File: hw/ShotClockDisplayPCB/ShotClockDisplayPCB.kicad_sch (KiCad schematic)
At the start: 0 parts

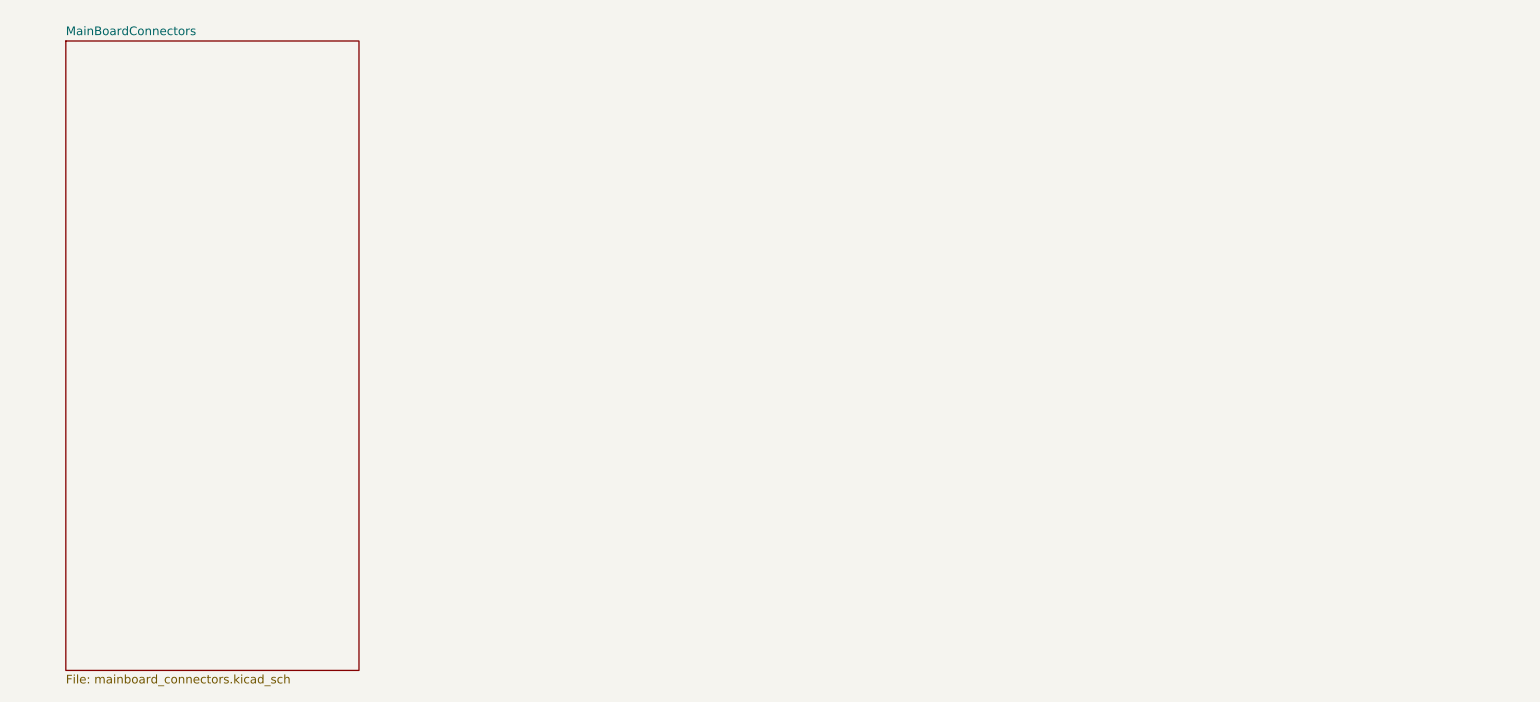
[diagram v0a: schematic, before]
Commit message: Started on second PCB, and added 5V regulator
5V regulator added to main pcb for the segment displays, using same TPS63000 chip, but with a different selector resistor to choose for 5V

Added second project to contain the display PCBA design.

Calculated the current usage of the displays with different current limiting resistors on the LEDs.

Calculated the  current limit resistors for transistors behind LEDs
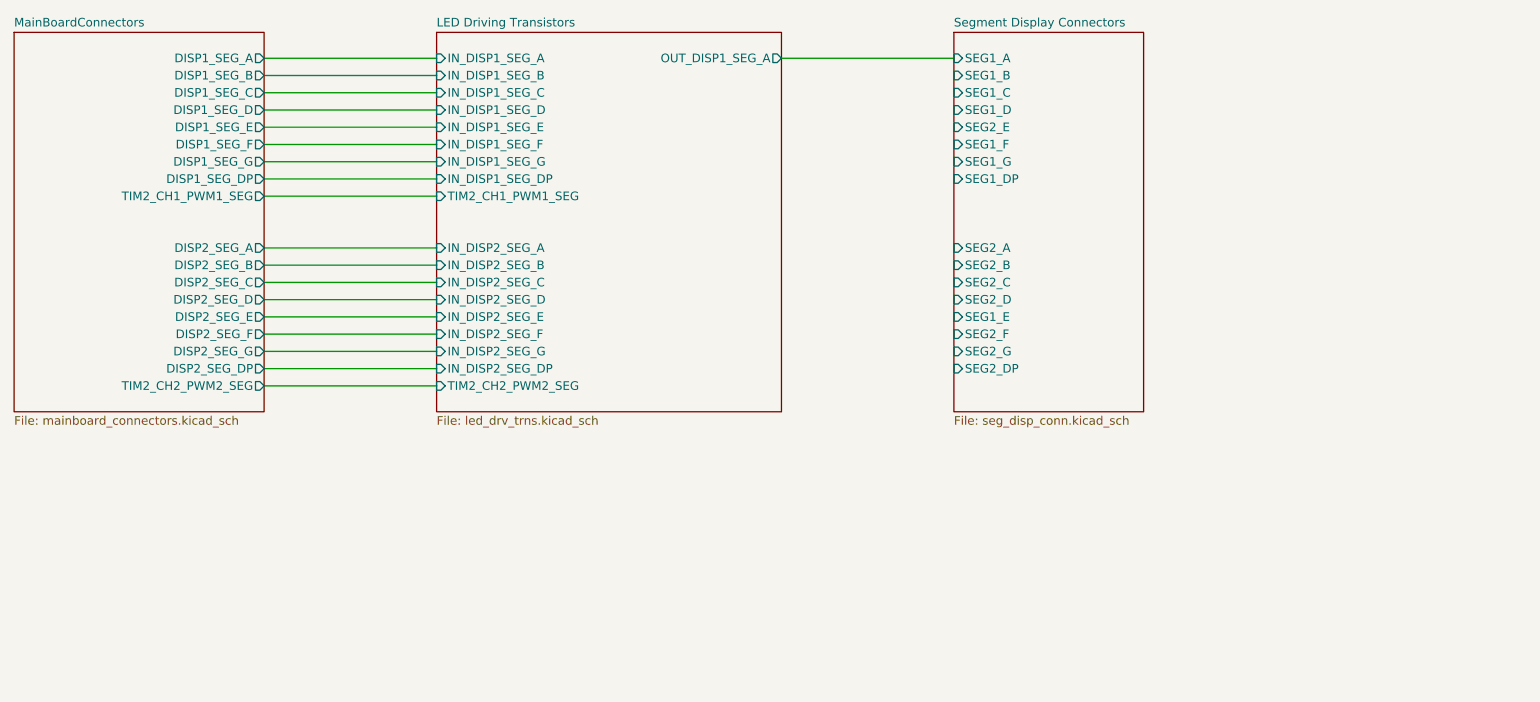
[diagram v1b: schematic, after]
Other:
- added sheet LED Driving Transistors (led_drv_trns.kicad_sch)
- added sheet Segment Display Connectors (seg_disp_conn.kicad_sch)
- sheet MainBoardConnectors ports: added DISP1_SEG_A, DISP1_SEG_B, DISP1_SEG_C, DISP1_SEG_D, DISP1_SEG_DP, DISP1_SEG_E, DISP1_SEG_F, DISP1_SEG_G, DISP2_SEG_A, DISP2_SEG_B, DISP2_SEG_C, DISP2_SEG_D, DISP2_SEG_DP, DISP2_SEG_E, DISP2_SEG_F, DISP2_SEG_G, TIM2_CH1_PWM1_SEG, TIM2_CH2_PWM2_SEG; removed none

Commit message: Finshed both schematics
- LED driving transistors are placed
- All connectors on segment display PCB are placed
- All schematic references have been re-configured (autosort on Y axis)
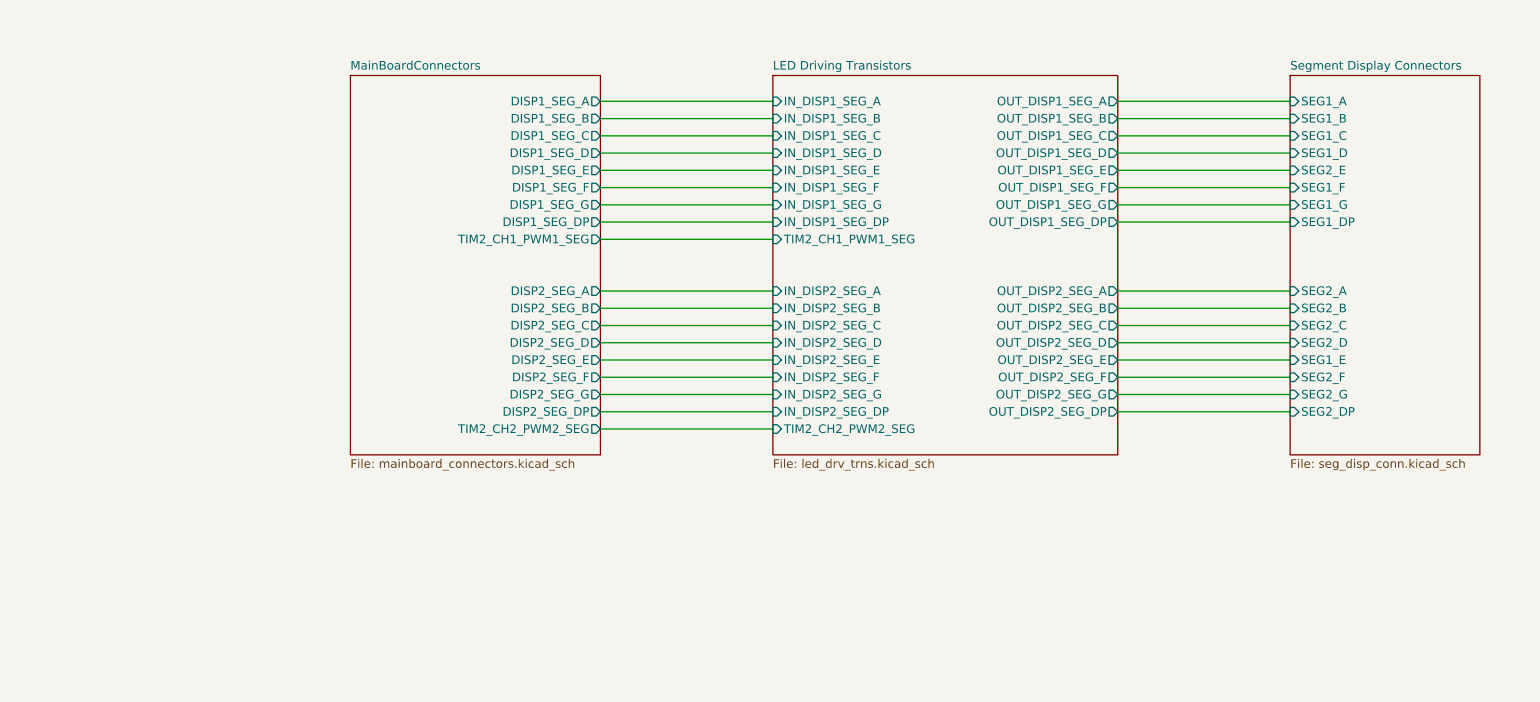
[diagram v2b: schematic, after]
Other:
- sheet LED Driving Transistors ports: added OUT_DISP1_SEG_B, OUT_DISP1_SEG_C, OUT_DISP1_SEG_D, OUT_DISP1_SEG_DP, OUT_DISP1_SEG_E, OUT_DISP1_SEG_F, OUT_DISP1_SEG_G, OUT_DISP2_SEG_A, OUT_DISP2_SEG_B, OUT_DISP2_SEG_C, OUT_DISP2_SEG_D, OUT_DISP2_SEG_DP, OUT_DISP2_SEG_E, OUT_DISP2_SEG_F, OUT_DISP2_SEG_G; removed none

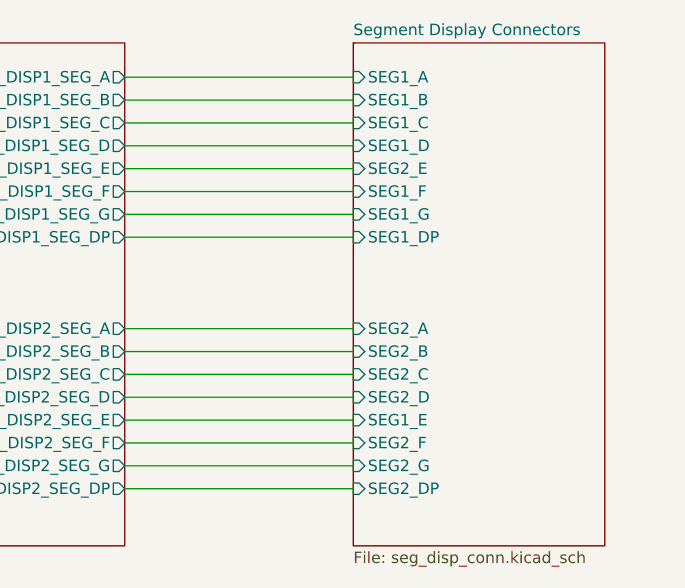
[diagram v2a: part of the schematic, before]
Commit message: Display print
Changed mainboard connector to FPC connector
Created routing for board
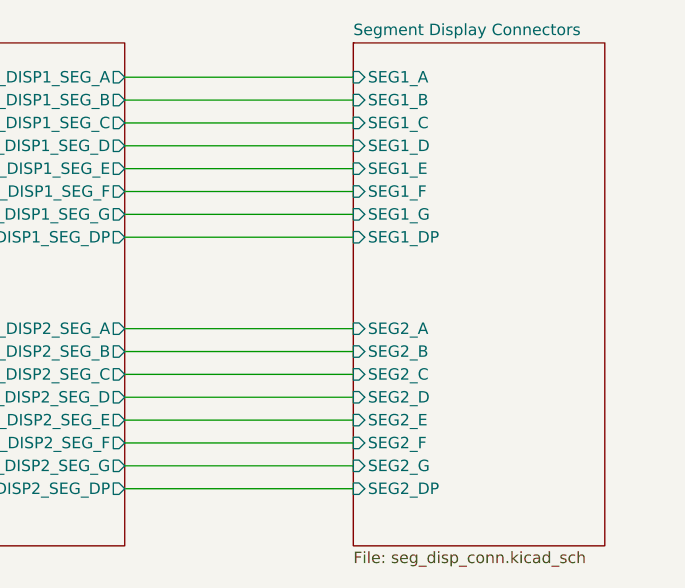
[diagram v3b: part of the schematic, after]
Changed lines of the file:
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@@
       (effects (font (size 1.27 1.27)) (justify left))
     )
-    (pin "SEG2_E" input (at 215.9 68.58 180)
+    (pin "SEG2_E" input (at 215.9 96.52 180)
       (effects (font (size 1.27 1.27)) (justify left))
     )
-    (pin "SEG1_E" input (at 215.9 96.52 180)
+    (pin "SEG1_E" input (at 215.9 68.58 180)
       (effects (font (size 1.27 1.27)) (justify left))
     )

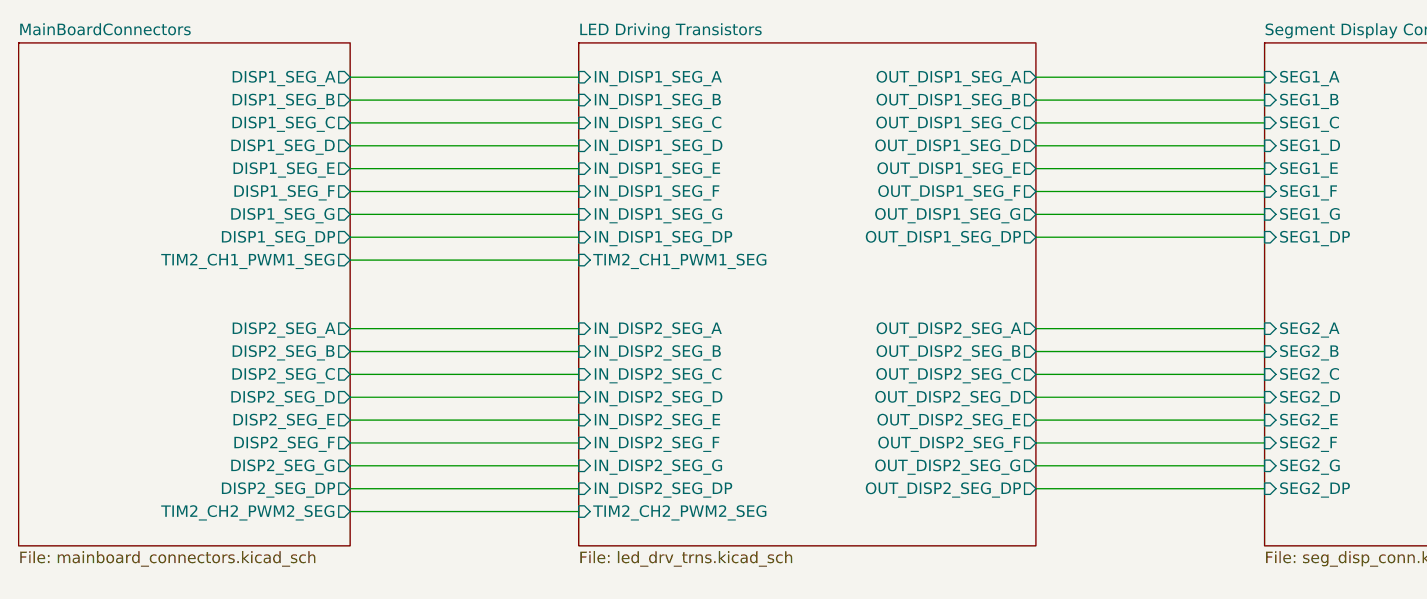
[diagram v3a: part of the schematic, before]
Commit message: Cleaned second print
and added new connectors, pinout and removed all REV1 stuff.
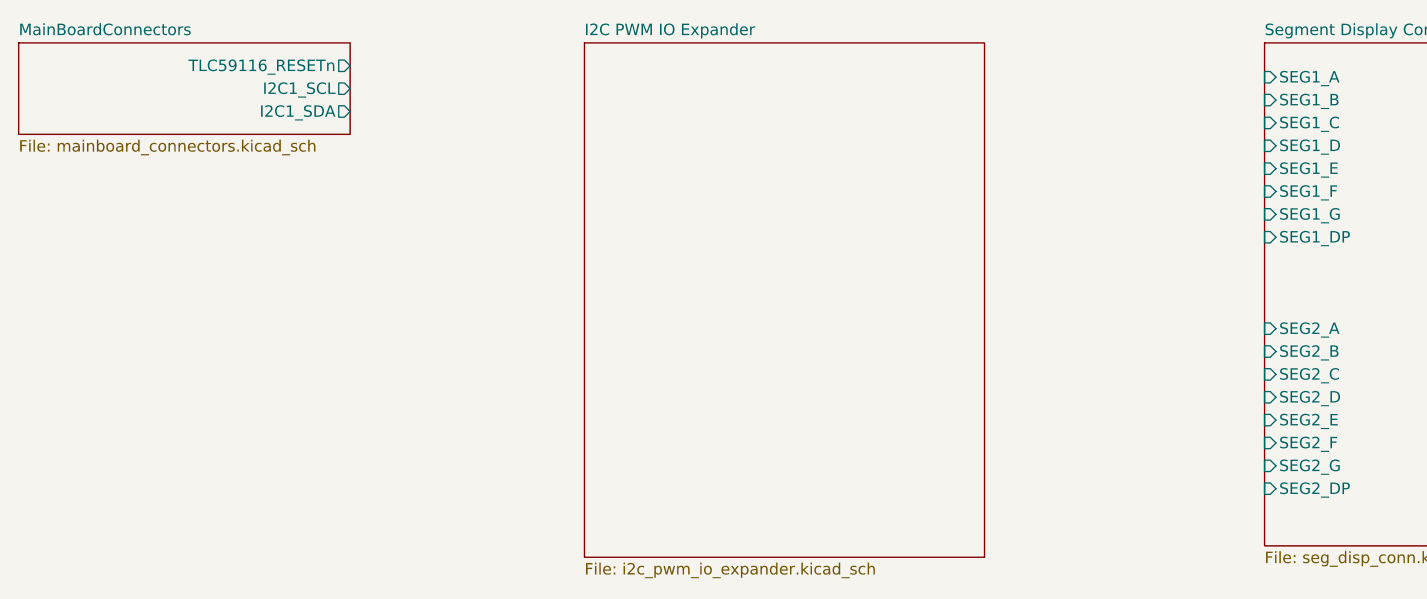
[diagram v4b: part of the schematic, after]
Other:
- removed sheet LED Driving Transistors
- added sheet I2C PWM IO Expander (i2c_pwm_io_expander.kicad_sch)
- sheet MainBoardConnectors ports: added I2C1_SCL, I2C1_SDA, TLC59116_RESETn; removed DISP1_SEG_A, DISP1_SEG_B, DISP1_SEG_C, DISP1_SEG_D, DISP1_SEG_DP, DISP1_SEG_E, DISP1_SEG_F, DISP1_SEG_G, DISP2_SEG_A, DISP2_SEG_B, DISP2_SEG_C, DISP2_SEG_D, DISP2_SEG_DP, DISP2_SEG_E, DISP2_SEG_F, DISP2_SEG_G, TIM2_CH1_PWM1_SEG, TIM2_CH2_PWM2_SEG

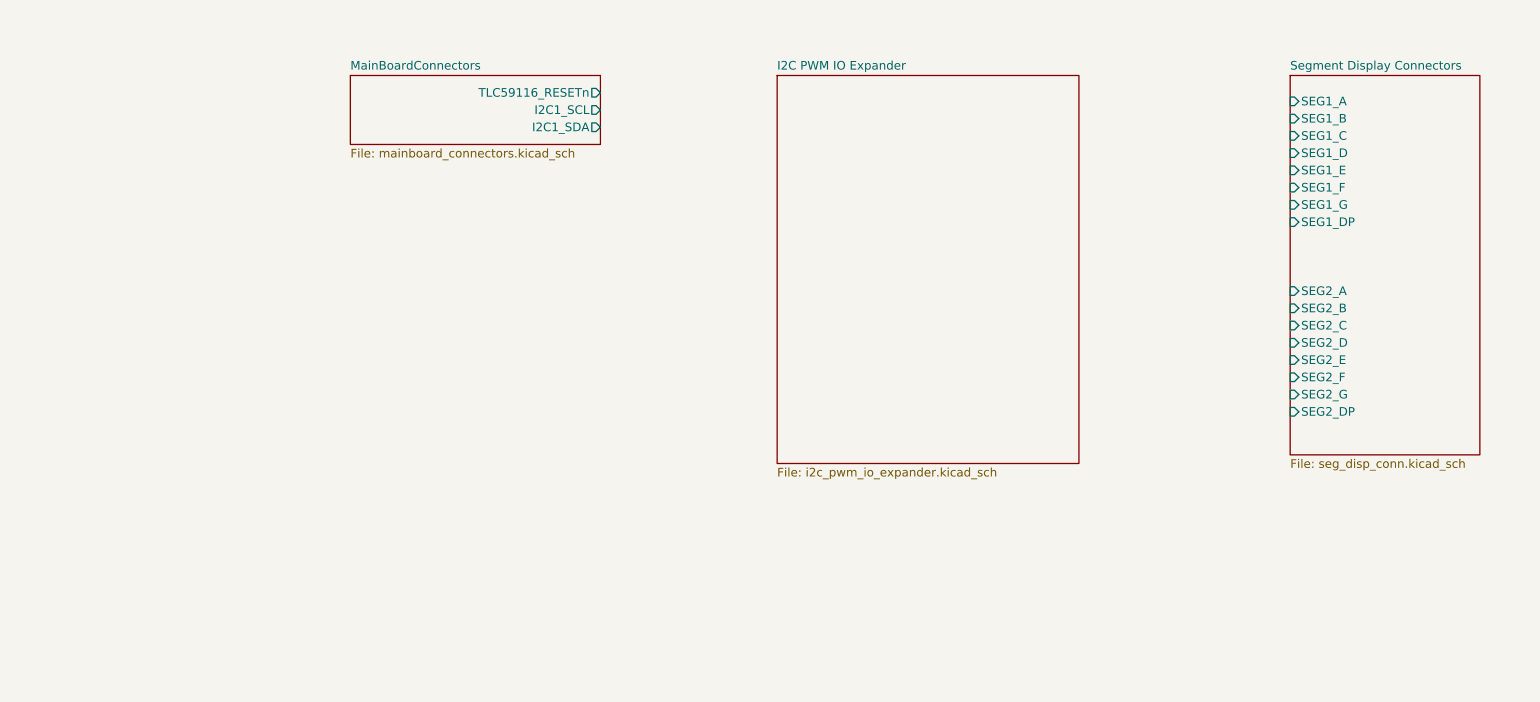
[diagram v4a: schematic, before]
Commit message: Started on display board rework
added new footprints
added HW select shunts/jumpers
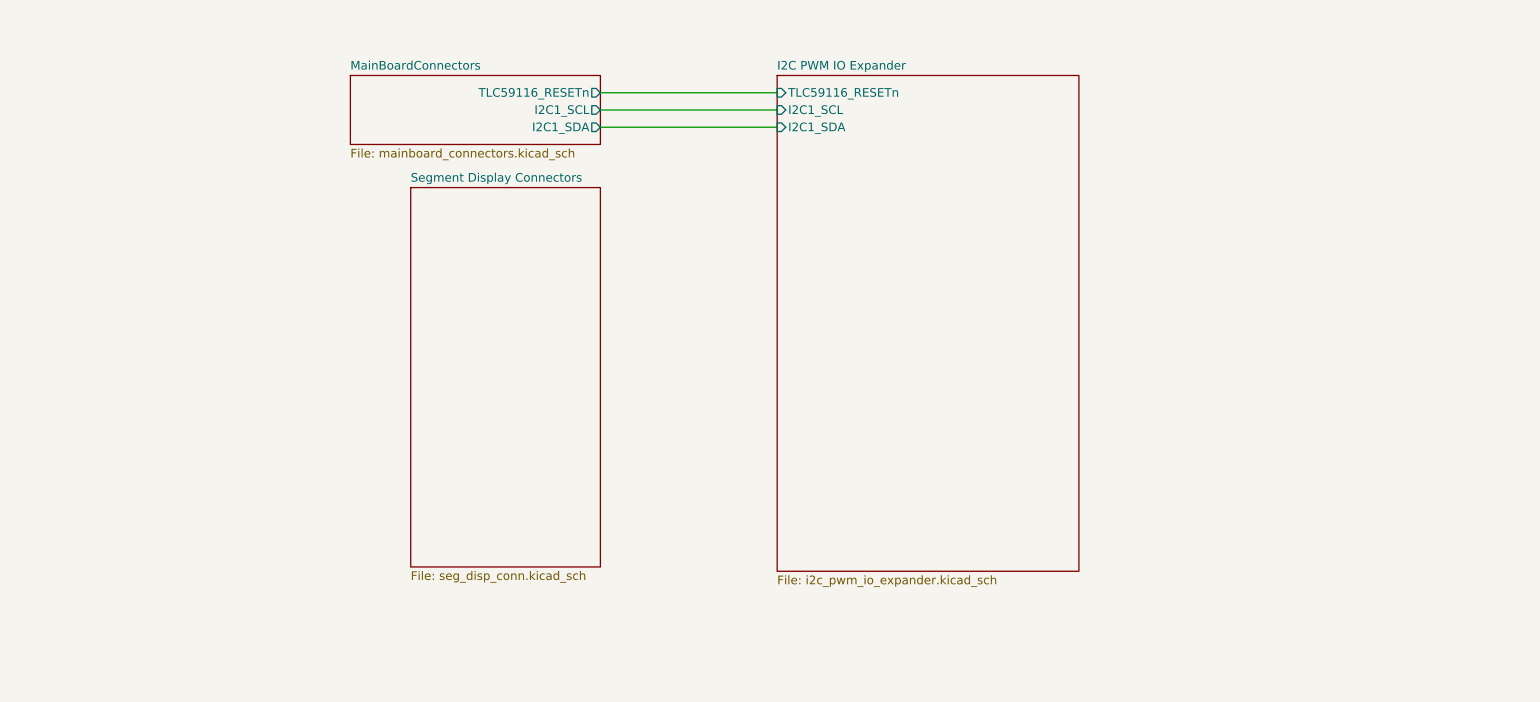
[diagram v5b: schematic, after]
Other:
- sheet I2C PWM IO Expander ports: added I2C1_SCL, I2C1_SDA, TLC59116_RESETn; removed none
- sheet Segment Display Connectors ports: added none; removed SEG1_A, SEG1_B, SEG1_C, SEG1_D, SEG1_DP, SEG1_E, SEG1_F, SEG1_G, SEG2_A, SEG2_B, SEG2_C, SEG2_D, SEG2_DP, SEG2_E, SEG2_F, SEG2_G
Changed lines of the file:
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@@
 (kicad_sch (version 20230121) (generator eeschema)
   (paper "A4")
-  (sheet (at 215.9 54.61) (size 27.94 55.88) (fields_autoplaced)
+  (wire (pts (xy 114.3 57.15) (xy 140.335 57.15))
+    (stroke (width 0) (type default))
+  )
+  (wire (pts (xy 114.3 59.69) (xy 140.335 59.69))
+    (stroke (width 0) (type default))
+  )
+  (wire (pts (xy 114.3 62.23) (xy 140.335 62.23))
+    (stroke (width 0) (type default))
+  )
+  (sheet (at 86.36 71.12) (size 27.94 55.88) (fields_autoplaced)
     (stroke (width 0.1524) (type solid))
     (fill (color 0 0 0 0.0000))
-    (property "Sheetname" "Segment Display Connectors" (at 215.9 53.8984 0)
+    (property "Sheetname" "Segment Display Connectors" (at 86.36 70.4084 0)
       (effects (font (size 1.27 1.27)) (justify left bottom))
     )
-    (property "Sheetfile" "seg_disp_conn.kicad_sch" (at 215.9 111.0746 0)
+    (property "Sheetfile" "seg_disp_conn.kicad_sch" (at 86.36 127.5846 0)
       (effects (font (size 1.27 1.27)) (justify left top))
-    )
-    (pin "SEG2_G" input (at 215.9 101.6 180)
-      (effects (font (size 1.27 1.27)) (justify left))
-    )
-    (pin "SEG2_A" input (at 215.9 86.36 180)
-      (effects (font (size 1.27 1.27)) (justify left))
-    )
-    (pin "SEG2_F" input (at 215.9 99.06 180)
-      (effects (font (size 1.27 1.27)) (justify left))
-    )
-    (pin "SEG2_B" input (at 215.9 88.9 180)
-      (effects (font (size 1.27 1.27)) (justify left))
-    )
-    (pin "SEG2_DP" input (at 215.9 104.14 180)
-      (effects (font (size 1.27 1.27)) (justify left))
-    )
-    (pin "SEG1_D" input (at 215.9 66.04 180)
-      (effects (font (size 1.27 1.27)) (justify left))
-    )
-    (pin "SEG1_C" input (at 215.9 63.5 180)
-      (effects (font (size 1.27 1.27)) (justify left))
-    )
-    (pin "SEG2_E" input (at 215.9 96.52 180)
-      (effects (font (size 1.27 1.27)) (justify left))
-    )
-    (pin "SEG1_E" input (at 215.9 68.58 180)
-      (effects (font (size 1.27 1.27)) (justify left))
-    )
-    (pin "SEG1_G" input (at 215.9 73.66 180)
-      (effects (font (size 1.27 1.27)) (justify left))
-    )
-    (pin "SEG1_A" input (at 215.9 58.42 180)
-      (effects (font (size 1.27 1.27)) (justify left))
-    )
-    (pin "SEG1_B" input (at 215.9 60.96 180)
-      (effects (font (size 1.27 1.27)) (justify left))
-    )
-    (pin "SEG1_DP" input (at 215.9 76.2 180)
-      (effects (font (size 1.27 1.27)) (justify left))
-    )
-    (pin "SEG1_F" input (at 215.9 71.12 180)
-      (effects (font (size 1.27 1.27)) (justify left))
-    )
-    (pin "SEG2_D" input (at 215.9 93.98 180)
-      (effects (font (size 1.27 1.27)) (justify left))
-    )
-    (pin "SEG2_C" input (at 215.9 91.44 180)
-      (effects (font (size 1.27 1.27)) (justify left))
     )
     (instances
@@
     )
   )
-  (sheet (at 140.335 54.61) (size 44.45 57.15) (fields_autoplaced)
+  (sheet (at 140.335 54.61) (size 44.45 73.025) (fields_autoplaced)
     (stroke (width 0.1524) (type solid))
     (fill (color 0 0 0 0.0000))
@@
       (effects (font (size 1.27 1.27)) (justify left bottom))
     )
-    (property "Sheetfile" "i2c_pwm_io_expander.kicad_sch" (at 140.335 112.3446 0)
+    (property "Sheetfile" "i2c_pwm_io_expander.kicad_sch" (at 140.335 128.2196 0)
       (effects (font (size 1.27 1.27)) (justify left top))
     )
+    (pin "I2C1_SDA" input (at 140.335 62.23 180)
+      (effects (font (size 1.27 1.27)) (justify left))
+    )
+    (pin "TLC59116_RESETn" input (at 140.335 57.15 180)
+      (effects (font (size 1.27 1.27)) (justify left))
+    )
+    (pin "I2C1_SCL" input (at 140.335 59.69 180)
+      (effects (font (size 1.27 1.27)) (justify left))
+    )
     (instances
